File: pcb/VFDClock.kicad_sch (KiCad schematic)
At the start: 2 parts, among them U1 SN74HC595PWR, U2 TBD62783AFWG

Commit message: Added custom VFD library
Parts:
- added B1: IV-22, Vacuum_Tubes:PL31-A_P_Socket, symbol Vacuum_Tubes:IV-22_VFD_Tube
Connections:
- net GND: now reaches U1.8 (GND)
- net GND: now also U2.10 (GND), B1.5
- net at U2.11 (O8): now also B1.1 (h)
- net at U2.12 (O7): now also B1.11 (g)
- net at U2.13 (O6): now also B1.2 (f)
- net at U2.14 (O5): now also B1.10 (e)
- net at U2.15 (O4): now also B1.3 (d)
- net at U2.16 (O3): now also B1.4 (c)
- net at U2.17 (O2): now also B1.8 (b)
- net at U2.18 (O1): now also B1.7 (a)
- no-connect marks 0 -> 1
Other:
- note removed: "Nakreslit socket footprint a symbol https://www.tube-tester.com/sites/nixie/dat_arch/IV-22.pdf"

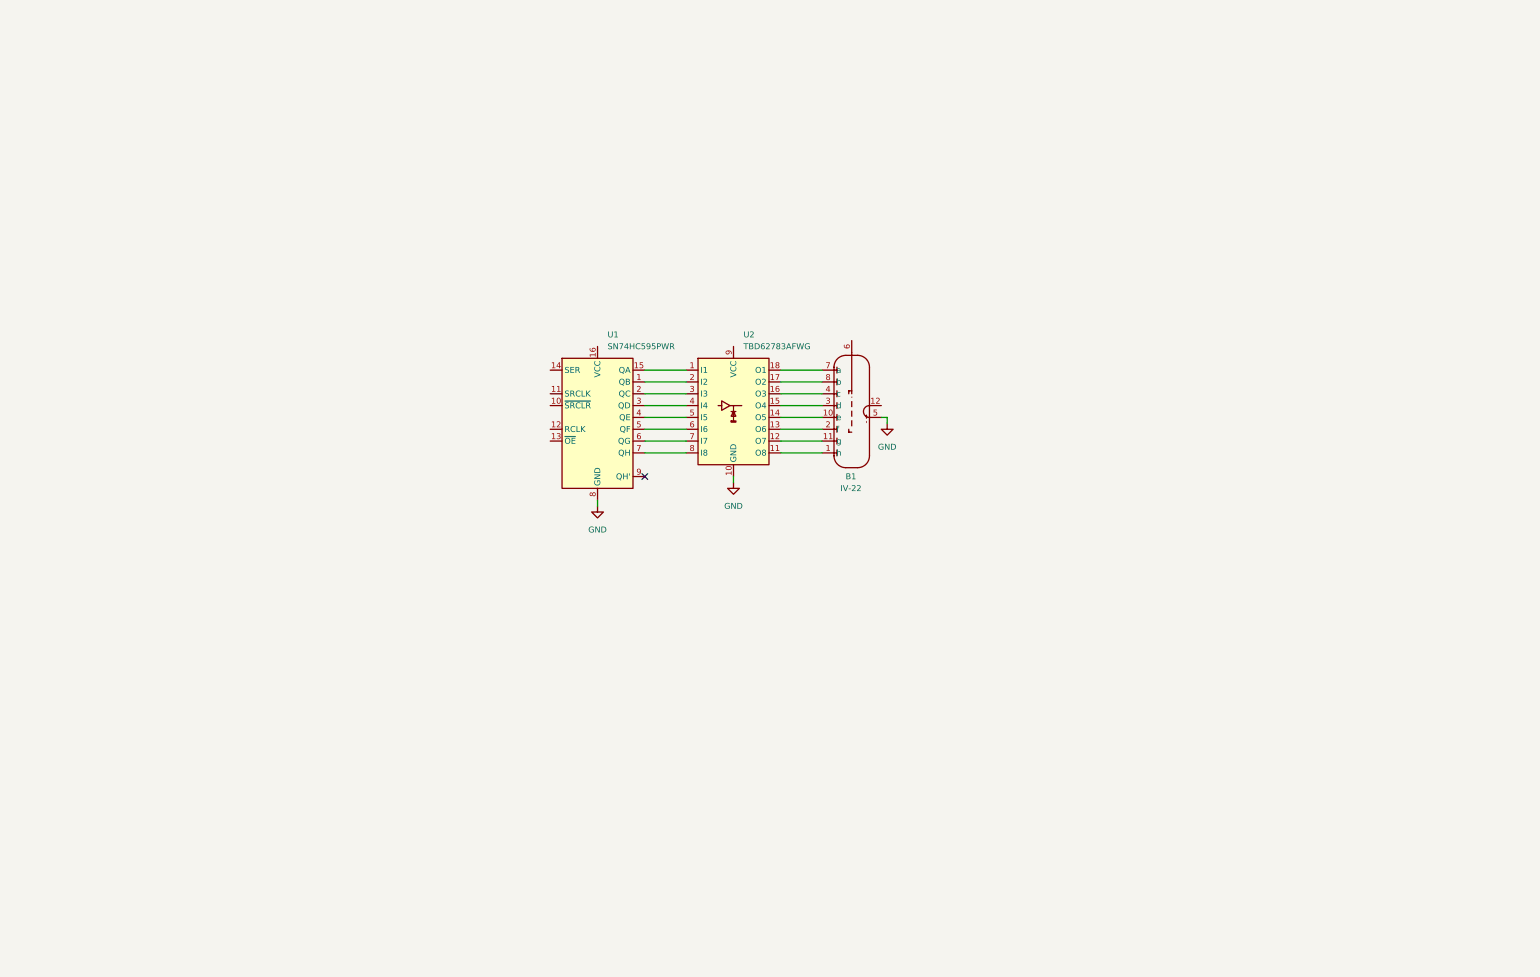
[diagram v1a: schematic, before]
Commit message: General schematic layout
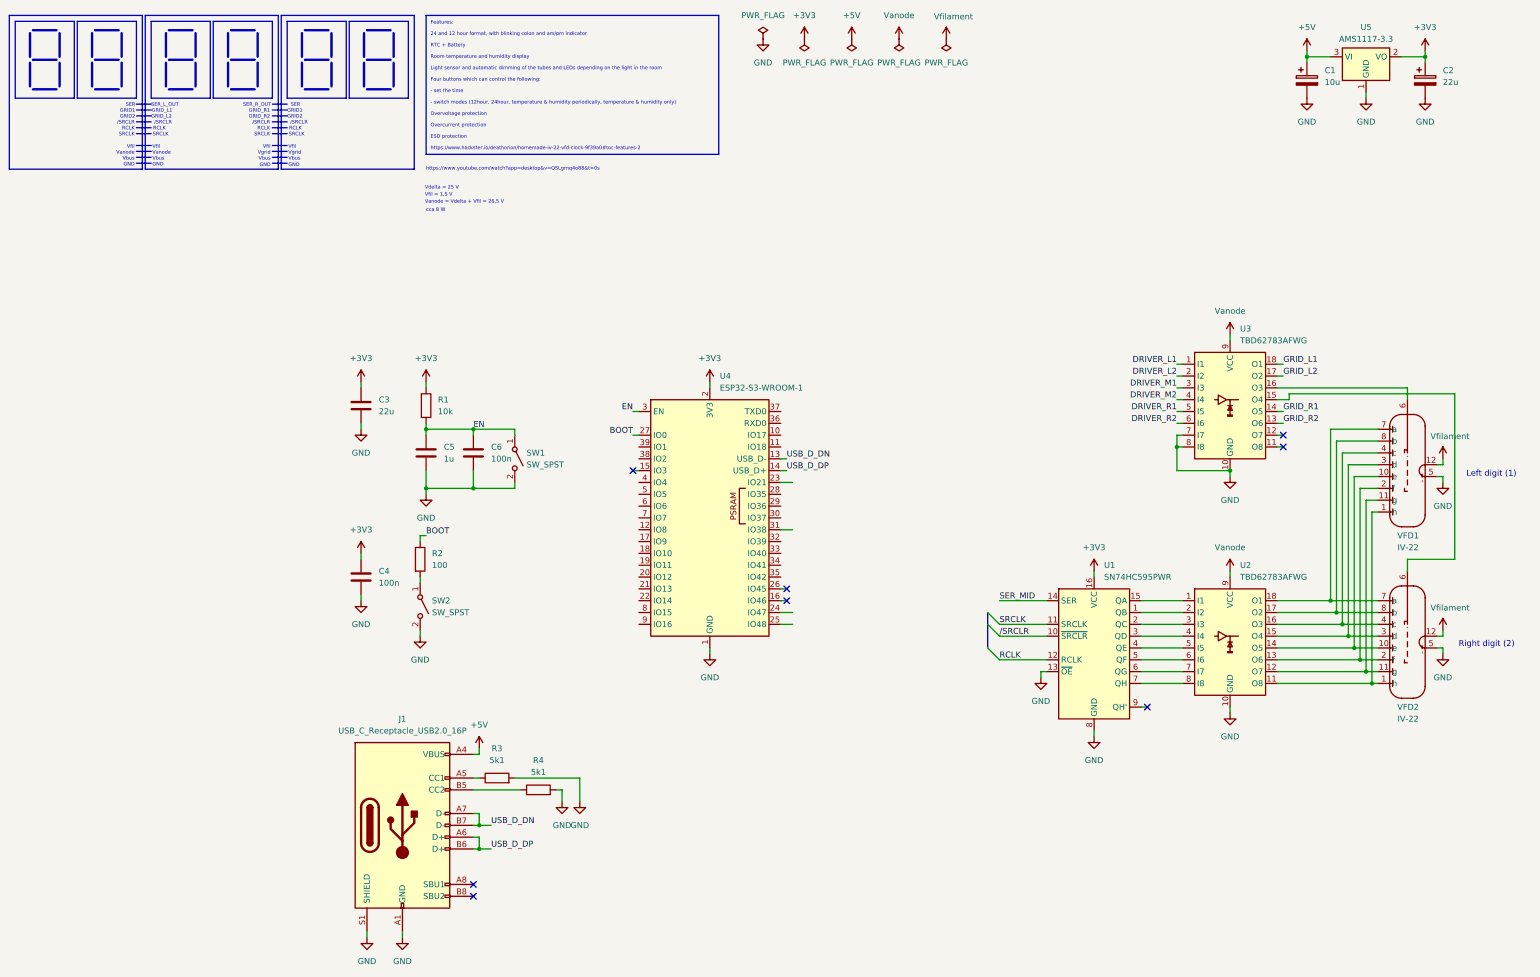
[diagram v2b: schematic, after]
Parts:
- removed B1: IV-22, Vacuum_Tubes:PL31-A_P_Socket, symbol Vacuum_Tubes:IV-22_VFD_Tube
- added C1: 10u, Capacitor_Tantalum_SMD:CP_EIA-3216-18_Kemet-A, symbol Device:C_Polarized
- added C2: 22u, Capacitor_Tantalum_SMD:CP_EIA-3528-15_AVX-H, symbol Device:C_Polarized
- added C3: 22u, Capacitor_SMD:C_0805_2012Metric, symbol Device:C
- added C4, C6: 100n, Capacitor_SMD:C_0805_2012Metric, symbol Device:C
- added C5: 1u, Capacitor_SMD:C_0805_2012Metric, symbol Device:C
- added J1: USB_C_Receptacle_USB2.0_16P, symbol Connector:USB_C_Receptacle_USB2.0_16P
- added R1: 10k, Resistor_SMD:R_0805_2012Metric, symbol Device:R
- added R2: 100, Resistor_SMD:R_0805_2012Metric, symbol Device:R
- added R3, R4: 5k1, Resistor_SMD:R_0805_2012Metric, symbol Device:R
- added SW1, SW2: SW_SPST, Button_Switch_SMD:SW_SPST_B3U-1000P, symbol Switch:SW_SPST
- added U3: TBD62783AFWG, symbol Transistor_Array:TBD62783A
- added U4: ESP32-S3-WROOM-1, RF_Module:ESP32-S3-WROOM-1, symbol RF_Module:ESP32-S3-WROOM-1
- added U5: AMS1117-3.3, Package_TO_SOT_SMD:SOT-223-3_TabPin2, symbol Regulator_Linear:AMS1117-3.3
- added VFD1, VFD2: IV-22, Vacuum_Tubes:PL31-A_P_Socket, symbol Vacuum_Tubes:IV-22_VFD_Tube
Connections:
- net GND: now also U1.13 (~{OE}), C1.2, C2.2, C3.2, C4.2, C5.2, C6.2, J1.A1 (GND), J1.A12 (GND), J1.B1 (GND), J1.B12 (GND), J1.S1 (SHIELD), R3.2, R4.2, SW1.2 (B), SW2.2 (B), U3.10 (GND), U3.7 (I7), U3.8 (I8), U4.1 (GND), U4.40 (GND), U4.41 (GND), U5.1 (GND), VFD1.5, VFD2.5
- net /SRCLR: now reaches U1.10 (~{SRCLR})
- net SRCLK: now reaches U1.11 (SRCLK)
- net RCLK: now reaches U1.12 (RCLK)
- net SER_MID: now reaches U1.14 (SER)
- net +3V3: now reaches U1.16 (VCC)
- net +3V3: now also C2.1, C3.1, C4.1, R1.1, U4.2 (3V3), U5.2 (VO)
- net at U2.11 (O8): now also VFD1.1 (h), VFD2.1 (h)
- net at U2.14 (O5): now also VFD1.10 (e), VFD2.10 (e)
- net at U2.12 (O7): now also VFD1.11 (g), VFD2.11 (g)
- net at U2.13 (O6): now also VFD1.2 (f), VFD2.2 (f)
- net at U2.15 (O4): now also VFD1.3 (d), VFD2.3 (d)
- net at U2.16 (O3): now also VFD1.4 (c), VFD2.4 (c)
- net at U2.18 (O1): now also VFD1.7 (a), VFD2.7 (a)
- net at U2.17 (O2): now also VFD1.8 (b), VFD2.8 (b)
- net Vanode: now reaches U2.9 (VCC)
- net Vanode: now also U3.9 (VCC)
- new net: R2.2, SW2.1 (A)
- new net: U3.15 (O4), VFD2.6
- new net: J1.A5 (CC1), R3.1
- new net: J1.B5 (CC2), R4.1
- new net: U3.16 (O3), VFD1.6
- new net +5V: C1.1, J1.A4 (VBUS), J1.A9 (VBUS), J1.B4 (VBUS), J1.B9 (VBUS), U5.3 (VI)
- new net BOOT: R2.1, U4.27 (IO0)
- new net DRIVER_L1: U3.1 (I1)
- new net DRIVER_L2: U3.2 (I2)
- new net DRIVER_M1: U3.3 (I3)
- new net DRIVER_M2: U3.4 (I4)
- new net DRIVER_R1: U3.5 (I5)
- new net DRIVER_R2: U3.6 (I6)
- new net EN: C5.1, C6.1, R1.2, SW1.1 (A), U4.3 (EN)
- new net GRID_L1: U3.18 (O1)
- new net GRID_L2: U3.17 (O2)
- new net GRID_R1: U3.14 (O5)
- new net GRID_R2: U3.13 (O6)
- new net USB_D_DN: J1.A7 (D-), J1.B7 (D-), U4.13 (USB_D-)
- new net USB_D_DP: J1.A6 (D+), J1.B6 (D+), U4.14 (USB_D+)
- new net Vfilament: VFD1.12, VFD2.12
- no-connect marks 1 -> 8
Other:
- note added: "/SRCLR"
- note added: "GND"
- note added: "GRID1"
- note added: "GRID2"
- note added: "GRID_L1"
- note added: "GRID_L2"
- note added: "GRID_R1"
- note added: "GRID_R2"
- note added: "Left digit (1)"
- note added: "RCLK"
- note added: "Right digit (2)"
- note added: "SER"
- note added: "SER_L_OUT"
- note added: "SER_R_OUT"
- note added: "SRCLK"
- note added: "Vanode"
- note added: "Vanode = Vdelta + Vfil = 26,5 V"
- note added: "Vbus"
- note added: "Vdelta = 25 V"
- note added: "Vfil"
- note added: "Vfil = 1,5 V"
- note added: "Vgrid"
- note added: "cca 8 W"
- note added: "https://www.youtube.com/watch?app=desktop&v=QSLgrnq4o88&t=0s"
- moved on the sheet: U1, U2

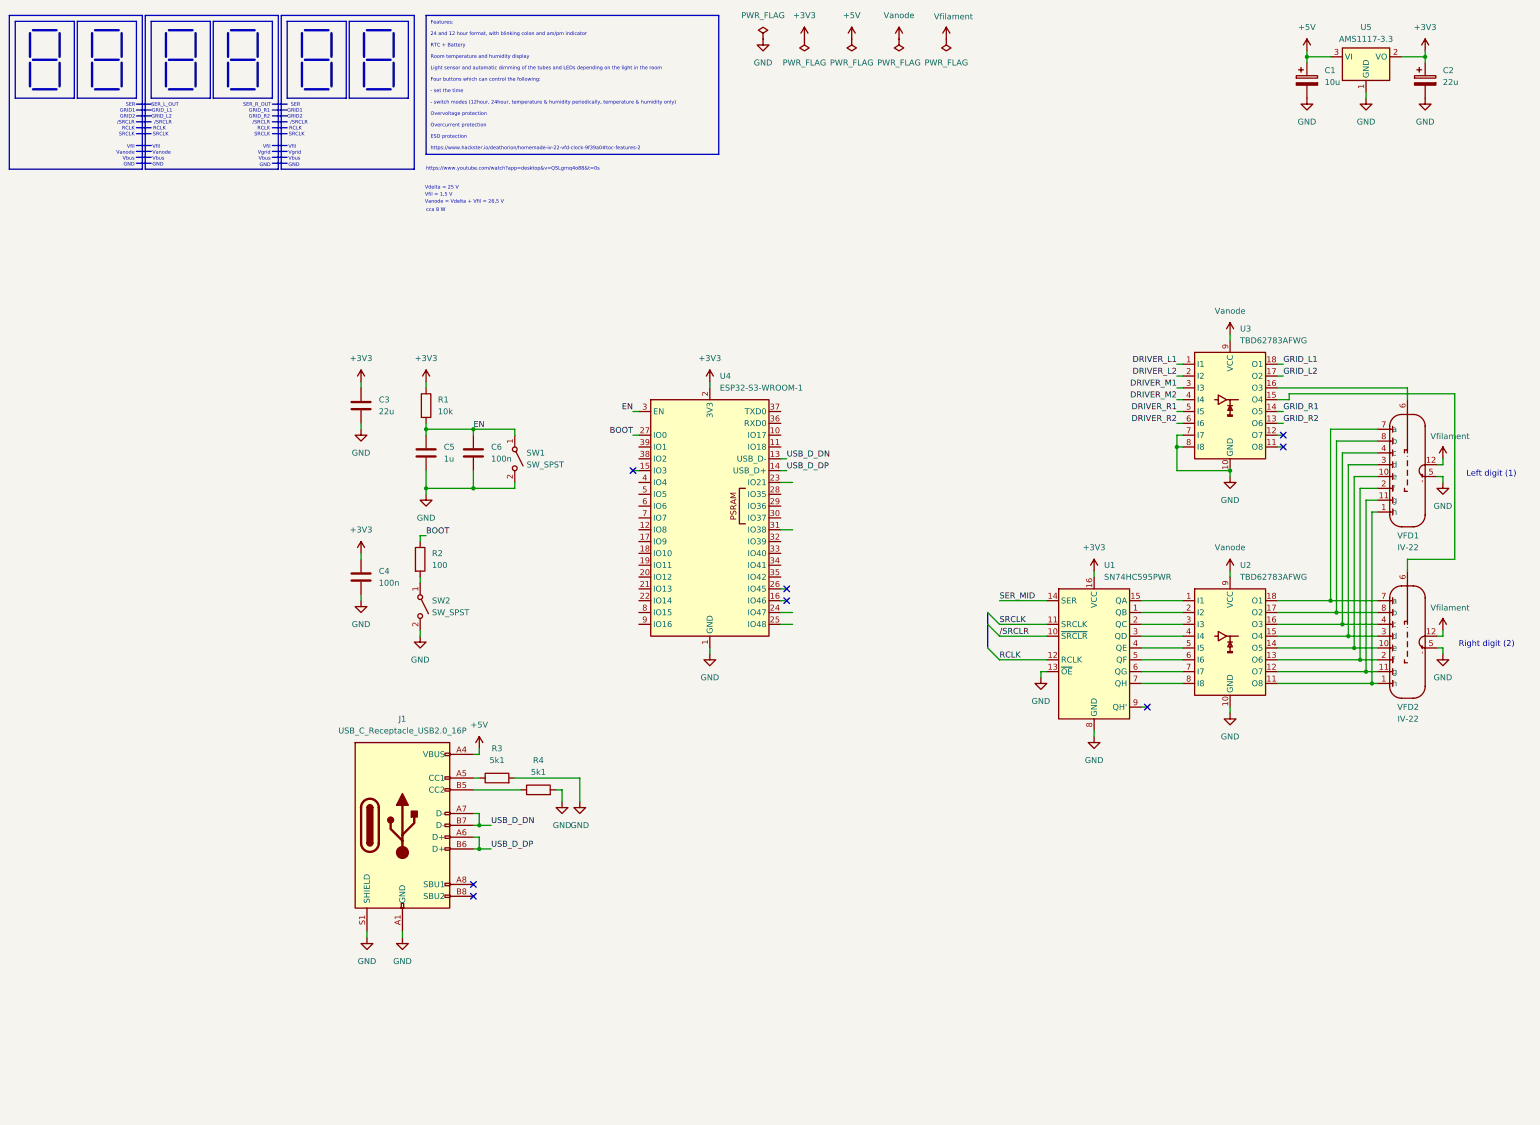
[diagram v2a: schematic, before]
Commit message: Added power supply part of schematic
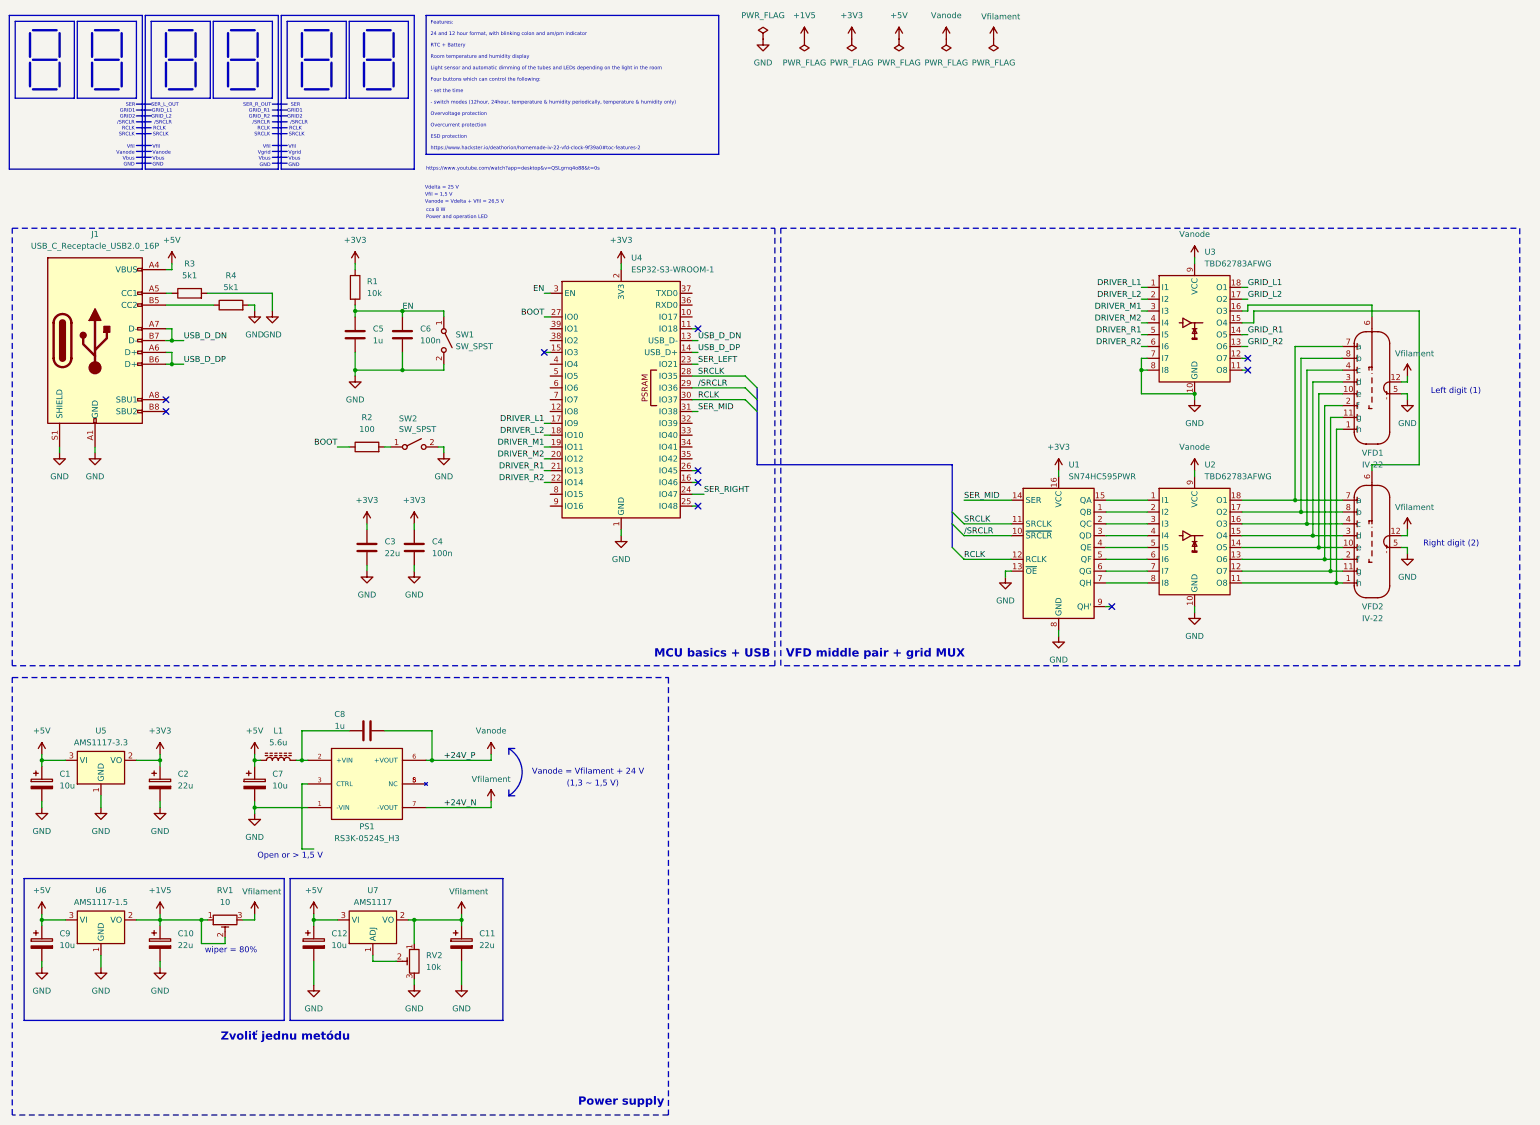
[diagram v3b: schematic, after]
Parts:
- added C10, C11: 22u, Capacitor_Tantalum_SMD:CP_EIA-3528-15_AVX-H, symbol Device:C_Polarized
- added C12, C7, C9: 10u, Capacitor_Tantalum_SMD:CP_EIA-3216-18_Kemet-A, symbol Device:C_Polarized
- added C8: 1u, Capacitor_SMD:C_0805_2012Metric, symbol Device:C
- added L1: 5.6u, Inductor_SMD:L_0201_0603Metric, symbol Device:L_Ferrite
- added PS1: RS3K-0524S_H3, VFDClock_custom_lib:CONV_RS3K-0524S_H3, symbol VFDClock_custom_lib:RS3K-0524S_H3
- added RV1: 10, symbol Device:R_Potentiometer_Trim
- added RV2: 10k, symbol Device:R_Potentiometer_Trim
- added U6: AMS1117-1.5, Package_TO_SOT_SMD:SOT-223-3_TabPin2, symbol Regulator_Linear:AMS1117-1.5
- added U7: AMS1117, Package_TO_SOT_SMD:SOT-223-3_TabPin2, symbol Regulator_Linear:AMS1117
- J1: footprint (none) -> Connector_USB:USB_C_Receptacle_GCT_USB4105-xx-A_16P_TopMnt_Horizontal
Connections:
- net +5V: now also C12.1, C7.1, C9.1, L1.1, U6.3 (VI), U7.3 (VI)
- net DRIVER_L1: now also U4.17 (IO9)
- net DRIVER_L2: now also U4.18 (IO10)
- net DRIVER_M1: now also U4.19 (IO11)
- net DRIVER_M2: now also U4.20 (IO12)
- net DRIVER_R1: now also U4.21 (IO13)
- net DRIVER_R2: now also U4.22 (IO14)
- net GND: now also C10.2, C11.2, C12.2, C7.2, C9.2, PS1.1 (-VIN), RV2.3, U6.1 (GND)
- net RCLK: now also U4.30 (IO37)
- net SER_MID: now also U4.31 (IO38)
- net SRCLK: now also U4.28 (IO35)
- net Vanode: now also C8.2, PS1.6 (+VOUT)
- net Vfilament: now also C11.1, PS1.7 (-VOUT), RV1.3, RV2.1, U7.2 (VO)
- net /SRCLR: now also U4.29 (IO36)
- net SER_LEFT: now reaches U4.23 (IO21)
- net SER_RIGHT: now reaches U4.24 (IO47)
- new net: C8.1, L1.2, PS1.2 (+VIN)
- new net: PS1.5 (NC), PS1.8 (NC)
- new net: RV2.2, U7.1 (ADJ)
- new net +1V5: C10.1, RV1.1, RV1.2, U6.2 (VO)
- no-connect marks 8 -> 10
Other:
- note added: "(1,3 ~ 1,5 V)"
- note added: "MCU basics + USB"
- note added: "Open or > 1,5 V"
- note added: "Power and operation LED"
- note added: "Power supply"
- note added: "VFD middle pair + grid MUX"
- note added: "Vanode = Vfilament + 24 V"
- note added: "Zvoliť jednu metódu"
- note added: "wiper = 80%"
- moved on the sheet: C1, C2, C3, C4, C5, C6, J1, R1, R3, R4, SW1, SW2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
